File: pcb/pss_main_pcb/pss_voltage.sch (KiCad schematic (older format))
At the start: 13 parts

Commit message: Fix schematics
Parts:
- gave numbers to parts that had none: 13

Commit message: Add footprints for power sources components
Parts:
- C1, C2: footprint (none) -> Capacitor_SMD:CP_Elec_16x17.5
- C3, C4: footprint (none) -> Capacitor_SMD:CP_Elec_8x10.5
- D1, D2: footprint (none) -> Diode_SMD:D_SMA_Handsoldering
- J1, J2: footprint (none) -> Connector_AMASS:AMASS_XT60-F_1x02_P7.20mm_Vertical
- L1, L2: footprint (none) -> Inductor_SMD:L_12x12mm_H8mm
- R1: footprint (none) -> Resistor_SMD:R_1206_3216Metric_Pad1.42x1.75mm_HandSolder
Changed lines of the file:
@@
 F 0 "J2" V 2710 4140 50  0000 L CNN
 F 1 "220V AC Input" V 2550 3850 50  0000 L CNN
-F 2 "" H 2650 4100 50  0001 C CNN
+F 2 "Connector_AMASS:AMASS_XT60-F_1x02_P7.20mm_Vertical" H 2650 4100 50  0001 C CNN
 F 3 "~" H 2650 4100 50  0001 C CNN
 	1    2650 4100
@@
 F 0 "J1" V 2710 2290 50  0000 L CNN
 F 1 "24V DC Input" V 2550 2000 50  0000 L CNN
-F 2 "" H 2650 2250 50  0001 C CNN
+F 2 "Connector_AMASS:AMASS_XT60-F_1x02_P7.20mm_Vertical" H 2650 2250 50  0001 C CNN
 F 3 "~" H 2650 2250 50  0001 C CNN
 	1    2650 2250
@@
 F 0 "C1" H 5850 2700 50  0000 L CNN
 F 1 "470u 50V" H 5500 2600 50  0000 L CNN
-F 2 "" H 6100 2650 50  0001 C CNN
+F 2 "Capacitor_SMD:CP_Elec_16x17.5" H 6100 2650 50  0001 C CNN
 F 3 "~" H 6100 2650 50  0001 C CNN
 	1    6100 2650
@@
 F 0 "L1" V 8050 2600 50  0000 C CNN
 F 1 "68u" V 8200 2600 50  0000 C CNN
-F 2 "" H 8100 2600 50  0001 C CNN
+F 2 "Inductor_SMD:L_12x12mm_H8mm" H 8100 2600 50  0001 C CNN
 F 3 "~" H 8100 2600 50  0001 C CNN
 	1    8100 2600
@@
 F 0 "D1" V 7654 2929 50  0000 L CNN
 F 1 "SS34" V 7745 2929 50  0000 L CNN
-F 2 "" H 7700 2850 50  0001 C CNN
+F 2 "Diode_SMD:D_SMA_Handsoldering" H 7700 2850 50  0001 C CNN
 F 3 "http://www.vishay.com/docs/88751/ss32.pdf" H 7700 2850 50  0001 C CNN
 	1    7700 2850
@@
 F 0 "C3" H 8765 2896 50  0000 L CNN
 F 1 "270u 10V" H 8765 2805 50  0000 L CNN
-F 2 "" H 8650 2850 50  0001 C CNN
+F 2 "Capacitor_SMD:CP_Elec_8x10.5" H 8650 2850 50  0001 C CNN
 F 3 "~" H 8650 2850 50  0001 C CNN
 	1    8650 2850
@@
 F 0 "R1" V 6293 3100 50  0000 C CNN
 F 1 "1k" V 6384 3100 50  0000 C CNN
-F 2 "" V 6430 3100 50  0001 C CNN
+F 2 "Resistor_SMD:R_1206_3216Metric_Pad1.42x1.75mm_HandSolder" V 6430 3100 50  0001 C CNN
 F 3 "~" H 6500 3100 50  0001 C CNN
 	1    6500 3100
@@
 F 0 "C2" H 5850 4600 50  0000 L CNN
 F 1 "470u 50V" H 5500 4500 50  0000 L CNN
-F 2 "" H 6100 4550 50  0001 C CNN
+F 2 "Capacitor_SMD:CP_Elec_16x17.5" H 6100 4550 50  0001 C CNN
 F 3 "~" H 6100 4550 50  0001 C CNN
 	1    6100 4550
@@
 F 0 "L2" V 8050 4500 50  0000 C CNN
 F 1 "47u" V 8200 4500 50  0000 C CNN
-F 2 "" H 8100 4500 50  0001 C CNN
+F 2 "Inductor_SMD:L_12x12mm_H8mm" H 8100 4500 50  0001 C CNN
 F 3 "~" H 8100 4500 50  0001 C CNN
 	1    8100 4500
@@
 F 0 "D2" V 7654 4829 50  0000 L CNN
 F 1 "SS34" V 7745 4829 50  0000 L CNN
-F 2 "" H 7700 4750 50  0001 C CNN
+F 2 "Diode_SMD:D_SMA_Handsoldering" H 7700 4750 50  0001 C CNN
 F 3 "http://www.vishay.com/docs/88751/ss32.pdf" H 7700 4750 50  0001 C CNN
 	1    7700 4750
@@
 F 0 "C4" H 8765 4796 50  0000 L CNN
 F 1 "330u 10V" H 8765 4705 50  0000 L CNN
-F 2 "" H 8650 4750 50  0001 C CNN
+F 2 "Capacitor_SMD:CP_Elec_8x10.5" H 8650 4750 50  0001 C CNN
 F 3 "~" H 8650 4750 50  0001 C CNN
 	1    8650 4750

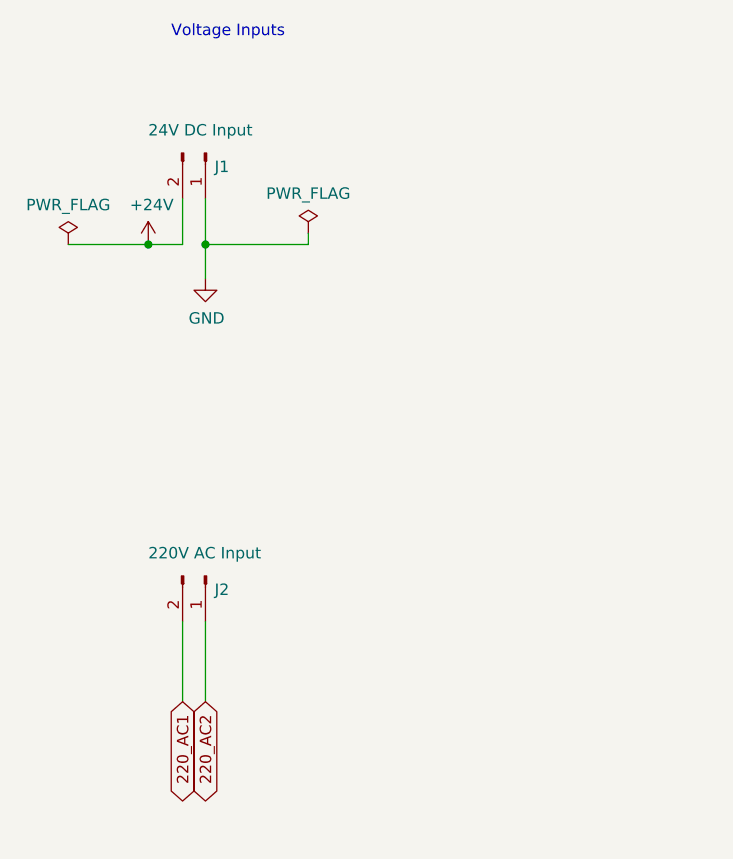
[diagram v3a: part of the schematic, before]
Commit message: Add footprints for heaters controls
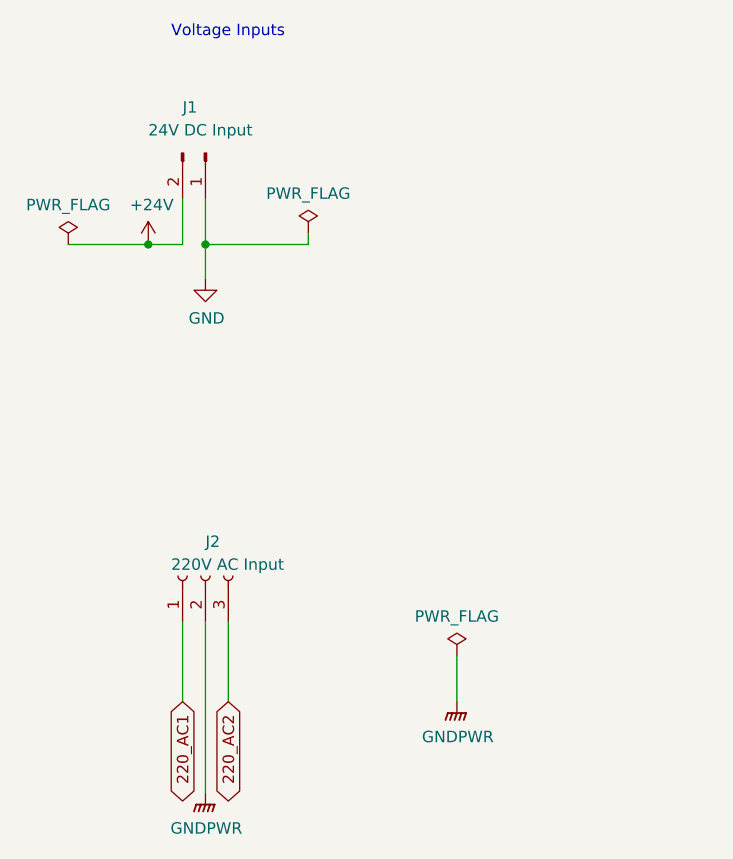
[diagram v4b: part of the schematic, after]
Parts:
- removed J2: 220V AC Input, Connector_AMASS:AMASS_XT60-F_1x02_P7.20mm_Vertical, symbol Connector:Conn_01x02_Male
- added J2: 220V AC Input, Connector:Banana_Jack_3Pin, symbol Connector:Conn_01x03_Female
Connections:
- net 220_AC1: now also J2.1 (Pin_1)
- net 220_AC2: now also J2.3 (Pin_3)
- new net GNDPWR: J2.2 (Pin_2)
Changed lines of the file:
@@
 	1    0    0    -1
-$EndComp
-$Comp
-L Connector:Conn_01x02_Male J?
-U 1 1 5EDC5C73
-P 2650 4100
-AR Path="/5EDC5C73" Ref="J?"  Part="1"
-AR Path="/5ED9AD16/5EDC5C73" Ref="J2"  Part="1"
-F 0 "J2" V 2710 4140 50  0000 L CNN
-F 1 "220V AC Input" V 2550 3850 50  0000 L CNN
-F 2 "Connector_AMASS:AMASS_XT60-F_1x02_P7.20mm_Vertical" H 2650 4100 50  0001 C CNN
-F 3 "~" H 2650 4100 50  0001 C CNN
-	1    2650 4100
-	0    1    1    0
 $EndComp
 Text GLabel 2550 4650 3    50   BiDi ~ 0
 220_AC1
-Text GLabel 2650 4650 3    50   BiDi ~ 0
-220_AC2
 $Comp
 L Connector:Conn_01x02_Male J?
@@
 AR Path="/5EDC5C90" Ref="J?"  Part="1"
 AR Path="/5ED9AD16/5EDC5C90" Ref="J1"  Part="1"
-F 0 "J1" V 2710 2290 50  0000 L CNN
+F 0 "J1" V 2450 2150 50  0000 L CNN
 F 1 "24V DC Input" V 2550 2000 50  0000 L CNN
 F 2 "Connector_AMASS:AMASS_XT60-F_1x02_P7.20mm_Vertical" H 2650 2250 50  0001 C CNN
@@
 	8900 4500 9250 4500
 Wire Wire Line
-	2650 4300 2650 4650
-Wire Wire Line
 	2550 4300 2550 4650
 $Comp
@@
 Wire Wire Line
 	2650 2650 2650 2800
+$Comp
+L Connector:Conn_01x03_Female J2
+U 1 1 5ECE2051
+P 2650 4100
+F 0 "J2" V 2800 4100 50  0000 R CNN
+F 1 "220V AC Input" V 2700 4250 50  0000 R CNN
+F 2 "Connector:Banana_Jack_3Pin" H 2650 4100 50  0001 C CNN
+F 3 "~" H 2650 4100 50  0001 C CNN
+	1    2650 4100
+	0    -1   -1   0
+$EndComp
+Text GLabel 2750 4650 3    50   BiDi ~ 0
+220_AC2
+Wire Wire Line
+	2750 4650 2750 4300
+$Comp
+L power:GNDPWR #PWR01
+U 1 1 5ECE62C4
+P 2650 5050
+F 0 "#PWR01" H 2650 4850 50  0001 C CNN
+F 1 "GNDPWR" H 2654 4896 50  0000 C CNN
+F 2 "" H 2650 5000 50  0001 C CNN
+F 3 "" H 2650 5000 50  0001 C CNN
+	1    2650 5050
+	1    0    0    -1
+$EndComp
+Wire Wire Line
+	2650 5050 2650 4300
+$Comp
+L power:GNDPWR #PWR?
+U 1 1 5ED1418A
+P 3750 4650
+AR Path="/5EE1CBE0/5ED1418A" Ref="#PWR?"  Part="1"
+AR Path="/5ED9AD16/5ED1418A" Ref="#PWR02"  Part="1"
+F 0 "#PWR02" H 3750 4450 50  0001 C CNN
+F 1 "GNDPWR" H 3754 4496 50  0000 C CNN
+F 2 "" H 3750 4600 50  0001 C CNN
+F 3 "" H 3750 4600 50  0001 C CNN
+	1    3750 4650
+	1    0    0    -1
+$EndComp
+$Comp
+L power:PWR_FLAG #FLG?
+U 1 1 5ED14190
+P 3750 4450
+AR Path="/5EE1CBE0/5ED14190" Ref="#FLG?"  Part="1"
+AR Path="/5ED9AD16/5ED14190" Ref="#FLG01"  Part="1"
+F 0 "#FLG01" H 3750 4525 50  0001 C CNN
+F 1 "PWR_FLAG" H 3750 4623 50  0000 C CNN
+F 2 "" H 3750 4450 50  0001 C CNN
+F 3 "~" H 3750 4450 50  0001 C CNN
+	1    3750 4450
+	1    0    0    -1
+$EndComp
+Wire Wire Line
+	3750 4650 3750 4450
 $EndSCHEMATC

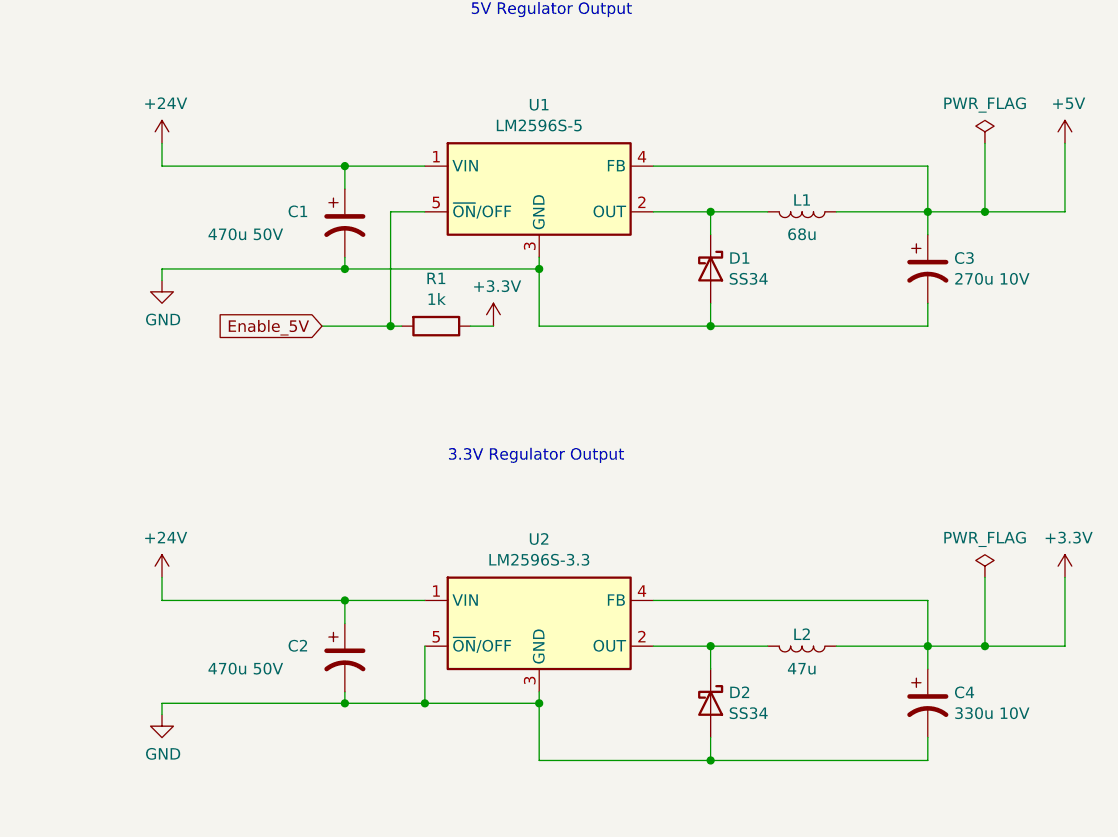
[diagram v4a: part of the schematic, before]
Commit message: Change footprints
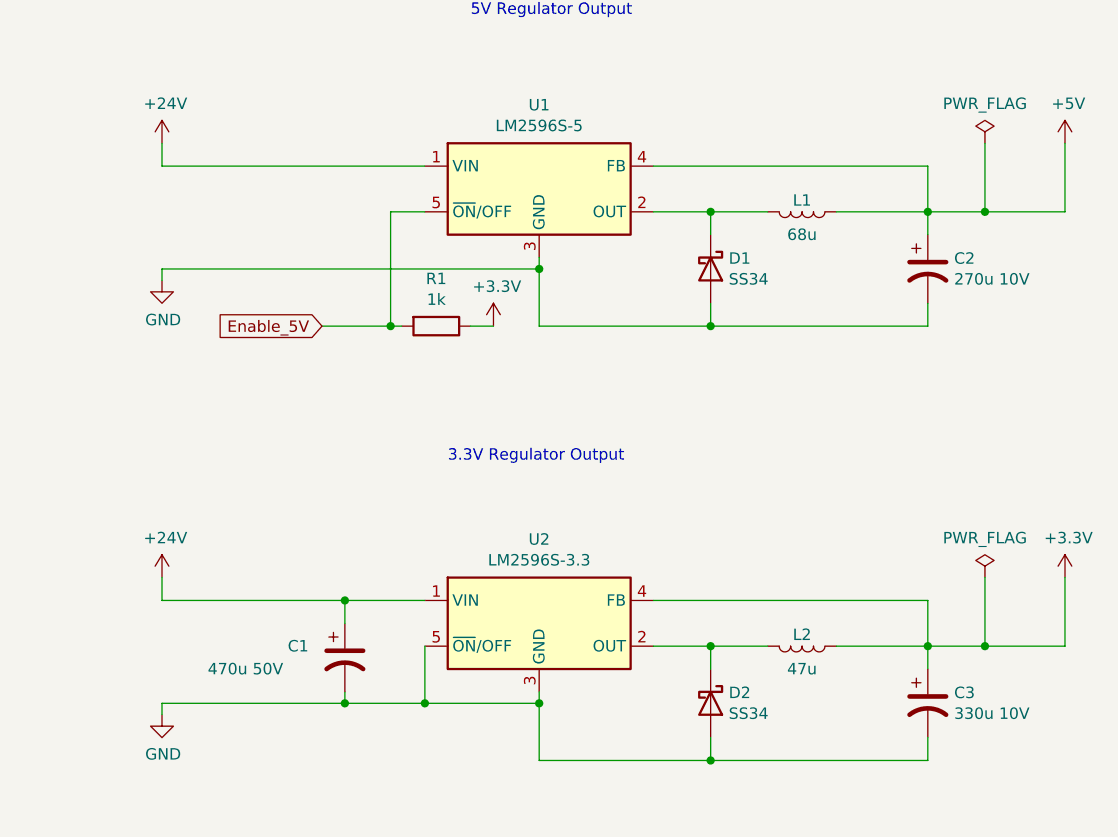
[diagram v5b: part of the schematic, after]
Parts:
- removed C1: 470u 50V, Capacitor_SMD:CP_Elec_16x17.5, symbol Device:CP1
- L1, L2: footprint Inductor_SMD:L_12x12mm_H8mm -> Inductor_SMD:L_Taiyo-Yuden_NR-30xx_HandSoldering
- renumbered C2 to C1, C3 to C2, C4 to C3
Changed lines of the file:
@@
 P 2400 2650
 AR Path="/5EDC5C6D" Ref="#PWR?"  Part="1"
-AR Path="/5ED9AD16/5EDC5C6D" Ref="#PWR0101"  Part="1"
-F 0 "#PWR0101" H 2400 2500 50  0001 C CNN
+AR Path="/5ED9AD16/5EDC5C6D" Ref="#PWR01"  Part="1"
+F 0 "#PWR01" H 2400 2500 50  0001 C CNN
 F 1 "+24V" H 2415 2823 50  0000 C CNN
 F 2 "" H 2400 2650 50  0001 C CNN
@@
 P 2650 2800
 AR Path="/5EDC5C97" Ref="#PWR?"  Part="1"
-AR Path="/5ED9AD16/5EDC5C97" Ref="#PWR0102"  Part="1"
-F 0 "#PWR0102" H 2650 2550 50  0001 C CNN
+AR Path="/5ED9AD16/5EDC5C97" Ref="#PWR02"  Part="1"
+F 0 "#PWR02" H 2650 2550 50  0001 C CNN
 F 1 "GND" H 2655 2627 50  0000 C CNN
 F 2 "" H 2650 2800 50  0001 C CNN
@@
 P 5300 2300
 AR Path="/5EDDCEC4" Ref="#PWR?"  Part="1"
-AR Path="/5ED9AD16/5EDDCEC4" Ref="#PWR0103"  Part="1"
-F 0 "#PWR0103" H 5300 2150 50  0001 C CNN
+AR Path="/5ED9AD16/5EDDCEC4" Ref="#PWR05"  Part="1"
+F 0 "#PWR05" H 5300 2150 50  0001 C CNN
 F 1 "+24V" H 5315 2473 50  0000 C CNN
 F 2 "" H 5300 2300 50  0001 C CNN
@@
 P 5300 2900
 AR Path="/5EDDCECA" Ref="#PWR?"  Part="1"
-AR Path="/5ED9AD16/5EDDCECA" Ref="#PWR0104"  Part="1"
-F 0 "#PWR0104" H 5300 2650 50  0001 C CNN
+AR Path="/5ED9AD16/5EDDCECA" Ref="#PWR06"  Part="1"
+F 0 "#PWR06" H 5300 2650 50  0001 C CNN
 F 1 "GND" H 5305 2727 50  0000 C CNN
 F 2 "" H 5300 2900 50  0001 C CNN
@@
 Wire Wire Line
 	5300 2300 5300 2400
-$Comp
-L Device:CP1 C?
-U 1 1 5EDDCED1
-P 6100 2650
-AR Path="/5EDDCED1" Ref="C?"  Part="1"
-AR Path="/5ED9AD16/5EDDCED1" Ref="C1"  Part="1"
-F 0 "C1" H 5850 2700 50  0000 L CNN
-F 1 "470u 50V" H 5500 2600 50  0000 L CNN
-F 2 "Capacitor_SMD:CP_Elec_16x17.5" H 6100 2650 50  0001 C CNN
-F 3 "~" H 6100 2650 50  0001 C CNN
-	1    6100 2650
-	1    0    0    -1
-$EndComp
-Wire Wire Line
-	6100 2400 6100 2500
 Wire Wire Line
 	5300 2900 5300 2850
-Wire Wire Line
-	5300 2850 6100 2850
-Wire Wire Line
-	6100 2850 6100 2800
-Wire Wire Line
-	5300 2400 6100 2400
 $Comp
 L Regulator_Switching:LM2596S-5 U?
@@
 $EndComp
 Wire Wire Line
-	6100 2400 6450 2400
-Connection ~ 6100 2400
-Connection ~ 6100 2850
-Wire Wire Line
 	6950 2800 6950 2850
 $Comp
@@
 F 0 "L1" V 8050 2600 50  0000 C CNN
 F 1 "68u" V 8200 2600 50  0000 C CNN
-F 2 "Inductor_SMD:L_12x12mm_H8mm" H 8100 2600 50  0001 C CNN
+F 2 "Inductor_SMD:L_Taiyo-Yuden_NR-30xx_HandSoldering" H 8100 2600 50  0001 C CNN
 F 3 "~" H 8100 2600 50  0001 C CNN
 	1    8100 2600
@@
 P 8650 2850
 AR Path="/5EDDCEF6" Ref="C?"  Part="1"
-AR Path="/5ED9AD16/5EDDCEF6" Ref="C3"  Part="1"
-F 0 "C3" H 8765 2896 50  0000 L CNN
+AR Path="/5ED9AD16/5EDDCEF6" Ref="C2"  Part="1"
+F 0 "C2" H 8765 2896 50  0000 L CNN
 F 1 "270u 10V" H 8765 2805 50  0000 L CNN
 F 2 "Capacitor_SMD:CP_Elec_8x10.5" H 8650 2850 50  0001 C CNN
@@
 P 9250 2300
 AR Path="/5EDDCF08" Ref="#PWR?"  Part="1"
-AR Path="/5ED9AD16/5EDDCF08" Ref="#PWR0105"  Part="1"
-F 0 "#PWR0105" H 9250 2150 50  0001 C CNN
+AR Path="/5ED9AD16/5EDDCF08" Ref="#PWR010"  Part="1"
+F 0 "#PWR010" H 9250 2150 50  0001 C CNN
 F 1 "+5V" H 9265 2473 50  0000 C CNN
 F 2 "" H 9250 2300 50  0001 C CNN
@@
 Text Notes 6650 1750 0    50   ~ 0
 5V Regulator Output
-Wire Wire Line
-	6100 2850 6950 2850
 $Comp
 L power:+3.3V #PWR?
@@
 P 6750 3100
 AR Path="/5EDDCF1B" Ref="#PWR?"  Part="1"
-AR Path="/5ED9AD16/5EDDCF1B" Ref="#PWR0106"  Part="1"
-F 0 "#PWR0106" H 6750 2950 50  0001 C CNN
+AR Path="/5ED9AD16/5EDDCF1B" Ref="#PWR09"  Part="1"
+F 0 "#PWR09" H 6750 2950 50  0001 C CNN
 F 1 "+3.3V" H 6765 3273 50  0000 C CNN
 F 2 "" H 6750 3100 50  0001 C CNN
@@
 P 5300 4200
 AR Path="/5EDEFDAE" Ref="#PWR?"  Part="1"
-AR Path="/5ED9AD16/5EDEFDAE" Ref="#PWR0107"  Part="1"
-F 0 "#PWR0107" H 5300 4050 50  0001 C CNN
+AR Path="/5ED9AD16/5EDEFDAE" Ref="#PWR07"  Part="1"
+F 0 "#PWR07" H 5300 4050 50  0001 C CNN
 F 1 "+24V" H 5315 4373 50  0000 C CNN
 F 2 "" H 5300 4200 50  0001 C CNN
@@
 P 5300 4800
 AR Path="/5EDEFDB4" Ref="#PWR?"  Part="1"
-AR Path="/5ED9AD16/5EDEFDB4" Ref="#PWR0108"  Part="1"
-F 0 "#PWR0108" H 5300 4550 50  0001 C CNN
+AR Path="/5ED9AD16/5EDEFDB4" Ref="#PWR08"  Part="1"
+F 0 "#PWR08" H 5300 4550 50  0001 C CNN
 F 1 "GND" H 5305 4627 50  0000 C CNN
 F 2 "" H 5300 4800 50  0001 C CNN
@@
 P 6100 4550
 AR Path="/5EDEFDBB" Ref="C?"  Part="1"
-AR Path="/5ED9AD16/5EDEFDBB" Ref="C2"  Part="1"
-F 0 "C2" H 5850 4600 50  0000 L CNN
+AR Path="/5ED9AD16/5EDEFDBB" Ref="C1"  Part="1"
+F 0 "C1" H 5850 4600 50  0000 L CNN
 F 1 "470u 50V" H 5500 4500 50  0000 L CNN
 F 2 "Capacitor_SMD:CP_Elec_16x17.5" H 6100 4550 50  0001 C CNN
@@
 F 0 "L2" V 8050 4500 50  0000 C CNN
 F 1 "47u" V 8200 4500 50  0000 C CNN
-F 2 "Inductor_SMD:L_12x12mm_H8mm" H 8100 4500 50  0001 C CNN
+F 2 "Inductor_SMD:L_Taiyo-Yuden_NR-30xx_HandSoldering" H 8100 4500 50  0001 C CNN
 F 3 "~" H 8100 4500 50  0001 C CNN
 	1    8100 4500
@@
 P 8650 4750
 AR Path="/5EDEFDDD" Ref="C?"  Part="1"
-AR Path="/5ED9AD16/5EDEFDDD" Ref="C4"  Part="1"
-F 0 "C4" H 8765 4796 50  0000 L CNN
+AR Path="/5ED9AD16/5EDEFDDD" Ref="C3"  Part="1"
+F 0 "C3" H 8765 4796 50  0000 L CNN
 F 1 "330u 10V" H 8765 4705 50  0000 L CNN
 F 2 "Capacitor_SMD:CP_Elec_8x10.5" H 8650 4750 50  0001 C CNN
@@
 P 9250 4200
 AR Path="/5EDEFE02" Ref="#PWR?"  Part="1"
-AR Path="/5ED9AD16/5EDEFE02" Ref="#PWR0109"  Part="1"
-F 0 "#PWR0109" H 9250 4050 50  0001 C CNN
+AR Path="/5ED9AD16/5EDEFE02" Ref="#PWR011"  Part="1"
+F 0 "#PWR011" H 9250 4050 50  0001 C CNN
 F 1 "+3.3V" H 9265 4373 50  0000 C CNN
 F 2 "" H 9250 4200 50  0001 C CNN
@@
 $EndComp
 $Comp
-L power:PWR_FLAG #FLG0103
+L power:PWR_FLAG #FLG01
 U 1 1 5ED37943
 P 2050 2650
-F 0 "#FLG0103" H 2050 2725 50  0001 C CNN
+F 0 "#FLG01" H 2050 2725 50  0001 C CNN
 F 1 "PWR_FLAG" H 2050 2823 50  0000 C CNN
 F 2 "" H 2050 2650 50  0001 C CNN
@@
 Connection ~ 2400 2650
 $Comp
-L power:PWR_FLAG #FLG0104
+L power:PWR_FLAG #FLG04
 U 1 1 5ED68CA1
 P 8900 2300
-F 0 "#FLG0104" H 8900 2375 50  0001 C CNN
+F 0 "#FLG04" H 8900 2375 50  0001 C CNN
 F 1 "PWR_FLAG" H 8900 2473 50  0000 C CNN
 F 2 "" H 8900 2300 50  0001 C CNN
@@
 	8900 2600 9250 2600
 $Comp
-L power:PWR_FLAG #FLG0105
+L power:PWR_FLAG #FLG05
 U 1 1 5ED6A98F
 P 8900 4200
-F 0 "#FLG0105" H 8900 4275 50  0001 C CNN
+F 0 "#FLG05" H 8900 4275 50  0001 C CNN
 F 1 "PWR_FLAG" H 8900 4373 50  0000 C CNN
 F 2 "" H 8900 4200 50  0001 C CNN
@@
 	2550 4300 2550 4650
 $Comp
-L power:PWR_FLAG #FLG0102
+L power:PWR_FLAG #FLG02
 U 1 1 5ED9A857
 P 3100 2600
-F 0 "#FLG0102" H 3100 2675 50  0001 C CNN
+F 0 "#FLG02" H 3100 2675 50  0001 C CNN
 F 1 "PWR_FLAG" H 3100 2773 50  0000 C CNN
 F 2 "" H 3100 2600 50  0001 C CNN
@@
 	2750 4650 2750 4300
 $Comp
-L power:GNDPWR #PWR01
+L power:GNDPWR #PWR03
 U 1 1 5ECE62C4
 P 2650 5050
-F 0 "#PWR01" H 2650 4850 50  0001 C CNN
+F 0 "#PWR03" H 2650 4850 50  0001 C CNN
 F 1 "GNDPWR" H 2654 4896 50  0000 C CNN
 F 2 "" H 2650 5000 50  0001 C CNN
@@
 P 3750 4650
 AR Path="/5EE1CBE0/5ED1418A" Ref="#PWR?"  Part="1"
-AR Path="/5ED9AD16/5ED1418A" Ref="#PWR02"  Part="1"
-F 0 "#PWR02" H 3750 4450 50  0001 C CNN
+AR Path="/5ED9AD16/5ED1418A" Ref="#PWR04"  Part="1"
+F 0 "#PWR04" H 3750 4450 50  0001 C CNN
 F 1 "GNDPWR" H 3754 4496 50  0000 C CNN
 F 2 "" H 3750 4600 50  0001 C CNN
@@
 P 3750 4450
 AR Path="/5EE1CBE0/5ED14190" Ref="#FLG?"  Part="1"
-AR Path="/5ED9AD16/5ED14190" Ref="#FLG01"  Part="1"
-F 0 "#FLG01" H 3750 4525 50  0001 C CNN
+AR Path="/5ED9AD16/5ED14190" Ref="#FLG03"  Part="1"
+F 0 "#FLG03" H 3750 4525 50  0001 C CNN
 F 1 "PWR_FLAG" H 3750 4623 50  0000 C CNN
 F 2 "" H 3750 4450 50  0001 C CNN
@@
 Wire Wire Line
 	3750 4650 3750 4450
+Wire Wire Line
+	5300 2400 6450 2400
+Wire Wire Line
+	5300 2850 6950 2850
 $EndSCHEMATC
